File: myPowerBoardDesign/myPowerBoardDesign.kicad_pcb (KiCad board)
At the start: 2 copper layers, 45 x 25 mm, 10 parts, among them J1 PowerBoard, U1 LM1117MP-3.3, U2 AP1509-50SG-13

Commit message: commit Apr 7 2024
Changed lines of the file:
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@@
 			(plot_on_all_layers_selection 0x0000000_00000000)
 			(disableapertmacros no)
-			(usegerberextensions no)
+			(usegerberextensions yes)
 			(usegerberattributes yes)
 			(usegerberadvancedattributes yes)
@@
 			(outputformat 1)
 			(mirror no)
-			(drillshape 1)
+			(drillshape 0)
 			(scaleselection 1)
-			(outputdirectory "")
+			(outputdirectory "Gerber/")
 		)
 	)
@@
 		(tags "capacitor handsolder")
 		(property "Reference" "C7"
-			(at 0 -1.85 270)
+			(at 0 -1.85 -90)
 			(layer "F.SilkS")
 			(effects
@@
 		)
 		(property "Value" "0.1u"
-			(at 0.8 1.45 270)
+			(at 0.8 1.45 -90)
 			(layer "F.Fab")
 			(effects
@@
 		)
 		(fp_text user "${REFERENCE}"
-			(at 0 0 270)
+			(at 0 0 -90)
 			(layer "F.Fab")
 			(effects
@@
 			(size 1.325 1.8)
 			(layers "F.Cu" "F.Paste" "F.Mask")
-			(roundrect_rratio 0.188679)
+			(roundrect_rratio 0.1886792453)
 			(net 2 "GND")
 			(pintype "passive")
@@
 			(size 1.325 1.8)
 			(layers "F.Cu" "F.Paste" "F.Mask")
-			(roundrect_rratio 0.188679)
+			(roundrect_rratio 0.1886792453)
 			(net 4 "+5V")
 			(pintype "passive")
@@
 		(tags "capacitor handsolder")
 		(property "Reference" "C2"
-			(at -3.55 -0.5 270)
+			(at -3.55 -0.5 -90)
 			(layer "F.SilkS")
 			(effects
@@
 			(size 1.325 1.8)
 			(layers "F.Cu" "F.Paste" "F.Mask")
-			(roundrect_rratio 0.188679)
+			(roundrect_rratio 0.1886792453)
 			(net 2 "GND")
 			(pintype "passive")
@@
 			(size 1.325 1.8)
 			(layers "F.Cu" "F.Paste" "F.Mask")
-			(roundrect_rratio 0.188679)
+			(roundrect_rratio 0.1886792453)
 			(net 1 "VIN")
 			(pintype "passive")
@@
 			(size 1.325 1.8)
 			(layers "F.Cu" "F.Paste" "F.Mask")
-			(roundrect_rratio 0.188679)
+			(roundrect_rratio 0.1886792453)
 			(net 2 "GND")
 			(pintype "passive")
@@
 			(size 1.325 1.8)
 			(layers "F.Cu" "F.Paste" "F.Mask")
-			(roundrect_rratio 0.188679)
+			(roundrect_rratio 0.1886792453)
 			(net 3 "+3V3")
 			(pintype "passive")
@@
 		(tags "Bourns SRN1060 SMD inductor")
 		(property "Reference" "L1"
-			(at 0 -6.2 270)
+			(at 0 -6.2 -90)
 			(layer "F.SilkS")
 			(effects
@@
 		)
 		(property "Value" "47u"
-			(at 0 6.2 270)
+			(at 0 6.2 -90)
 			(layer "F.Fab")
 			(effects
@@
 		)
 		(fp_text user "${REFERENCE}"
-			(at 0 0 270)
+			(at 0 0 -90)
 			(layer "F.Fab")
 			(effects
@@
 		(tags "SOP SO")
 		(property "Reference" "U2"
-			(at -2.6 -4 270)
+			(at -2.6 -4 -90)
 			(layer "F.SilkS")
 			(effects
@@
 		)
 		(property "Value" "AP1509-50SG-13"
-			(at 0 3.4 270)
+			(at 0 3.4 -90)
 			(layer "F.Fab")
 			(effects
@@
 		)
 		(fp_text user "${REFERENCE}"
-			(at 0 0 270)
-			(layer "F.Fab")
-			(effects
+			(at 0 0 -90)
+			(layer "F.Fab")
+			(effects

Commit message: Sat Apr 27: fixed a few things. Finalized v0.2 baseboard and powerboard. Added logos.
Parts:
- added G***: LOGO, logos:heritage-logo, B.Cu at (71.0, 50.5)
- moved C7 0.50 mm to (84.0, 52.8)
- moved C5 0.41 mm to (89.5, 39.6)
- moved C2 0.34 mm to (64.5, 56.2)
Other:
- board text added: "Hussam Al-Hertani Powerboard v0.2"

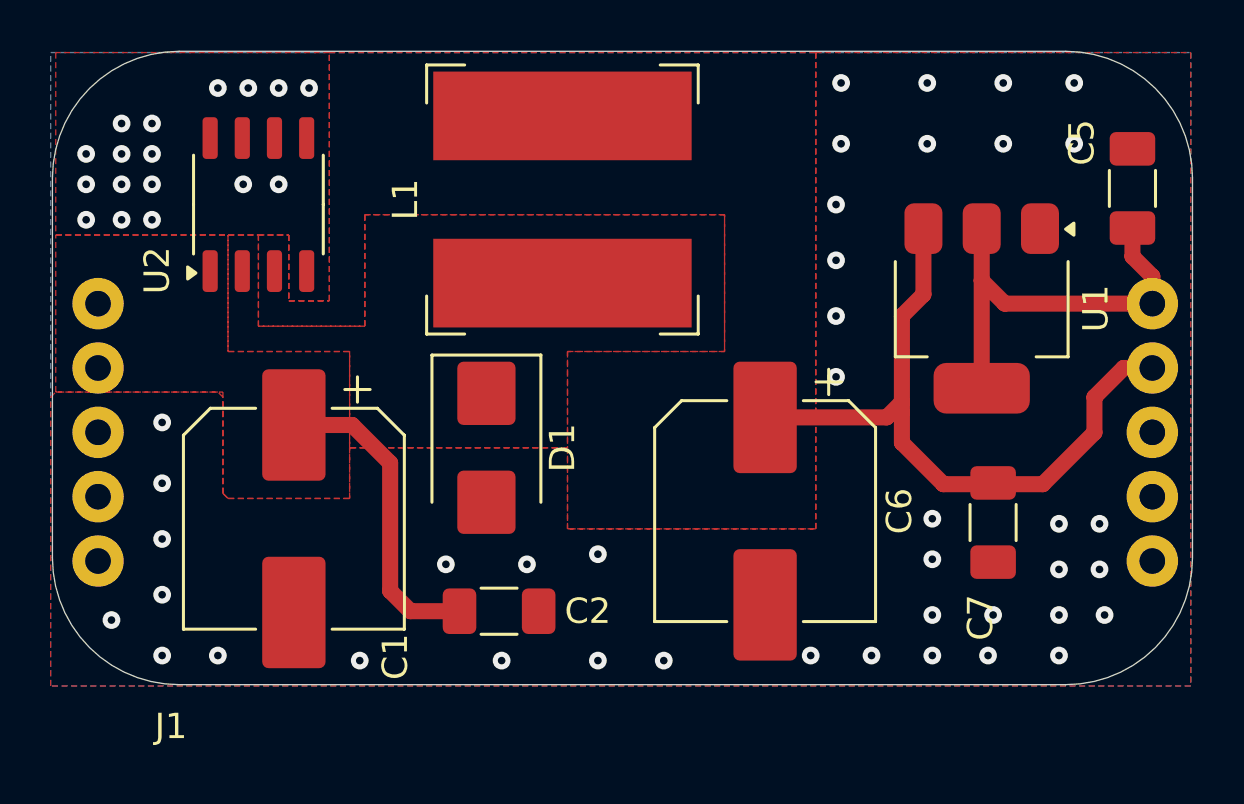
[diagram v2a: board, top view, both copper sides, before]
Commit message: created _latest gerber sets and added digikey boms. Also did some project cleanup WedMay82024
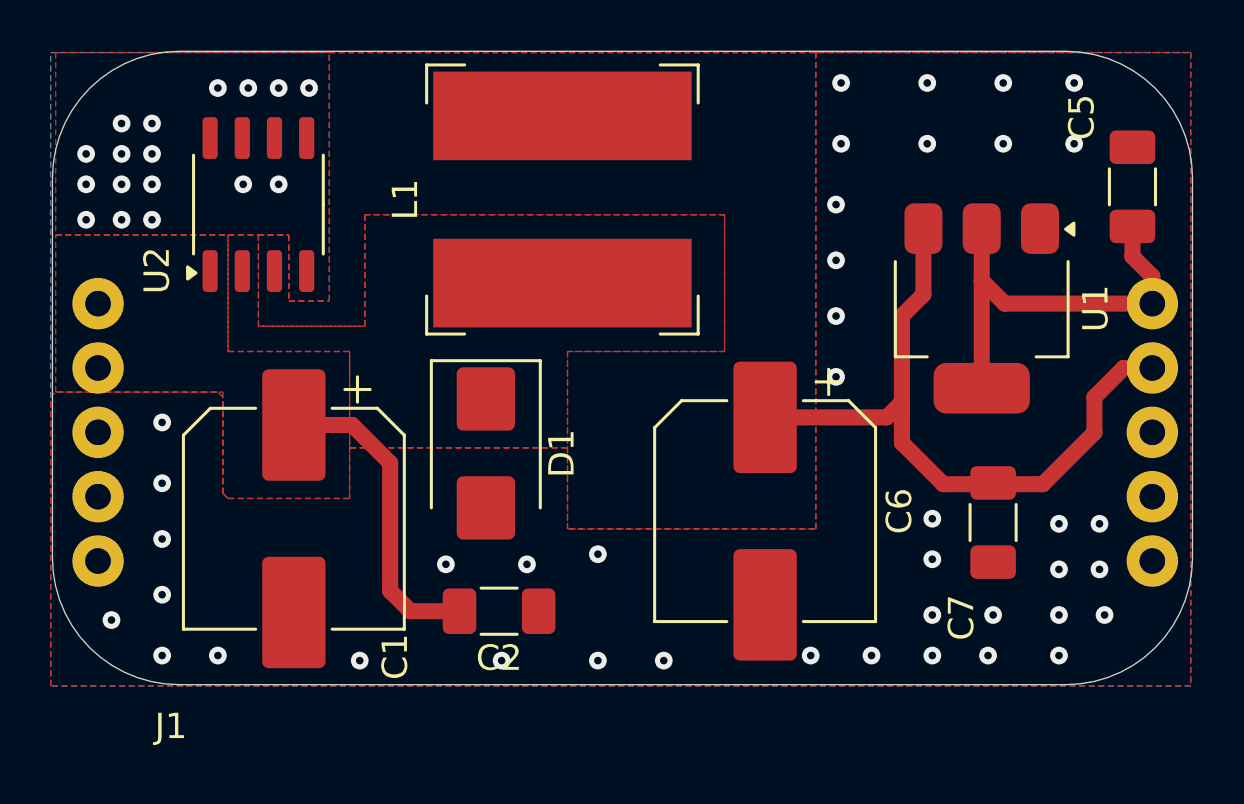
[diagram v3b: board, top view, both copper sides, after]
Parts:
- moved D1 0.22 mm to (64.0, 50.0)
- moved C5 0.06 mm to (89.5, 39.5)
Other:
- board text added: "+3V3"
- board text added: "+5V"
- board text added: "GND"
- board text added: "VIN"
